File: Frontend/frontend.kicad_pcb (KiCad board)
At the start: 4 copper layers, 100 x 100.2 mm, 355 parts, among them J1 VOCM, J10 SWD, J11 APWR, J2 BNC, J3 UMC, J4 UMC, J5 VOCM, J6 BNC, J7 UMC, J8 UMC, J9 PCIEx4 EDGE, K1 HE3600, K2 EE2-5NU, K3 HE3600, K4 HE3600, K5 EE2-5NU, K6 HE3600, Q1 ULN2003AD, U1 MCP9700T-E/TT, U10 ADA4817-1ACPZ, U11 MAX4567EEE, U12 MAX4567EEE, U13 MAX4567EEE, U14 AD8003ACPZ, U15 LMH6552SD, U16 MC33078DGK, U17 MAX5725AAUP, U18 STM32F030C8T, U19 MC33078DGK, U2 ADA4817-1ACPZ, U20 MC33078DGK, U21 MC33078DGK, U22 MC33078DGK, U23 LM317S, U24 MCP9700T-E/TT, U25 L78M05CDT, U26 TLV70233DSE, U27 MCP9700T-E/TT, U28 MC79M05CDT, U3 MAX4567EEE, U4 MAX4567EEE, U5 MAX4567EEE, U6 AD8003ACPZ, U7 LMH6552SD, U8 MC33078DGK, U9 MCP9700T-E/TT

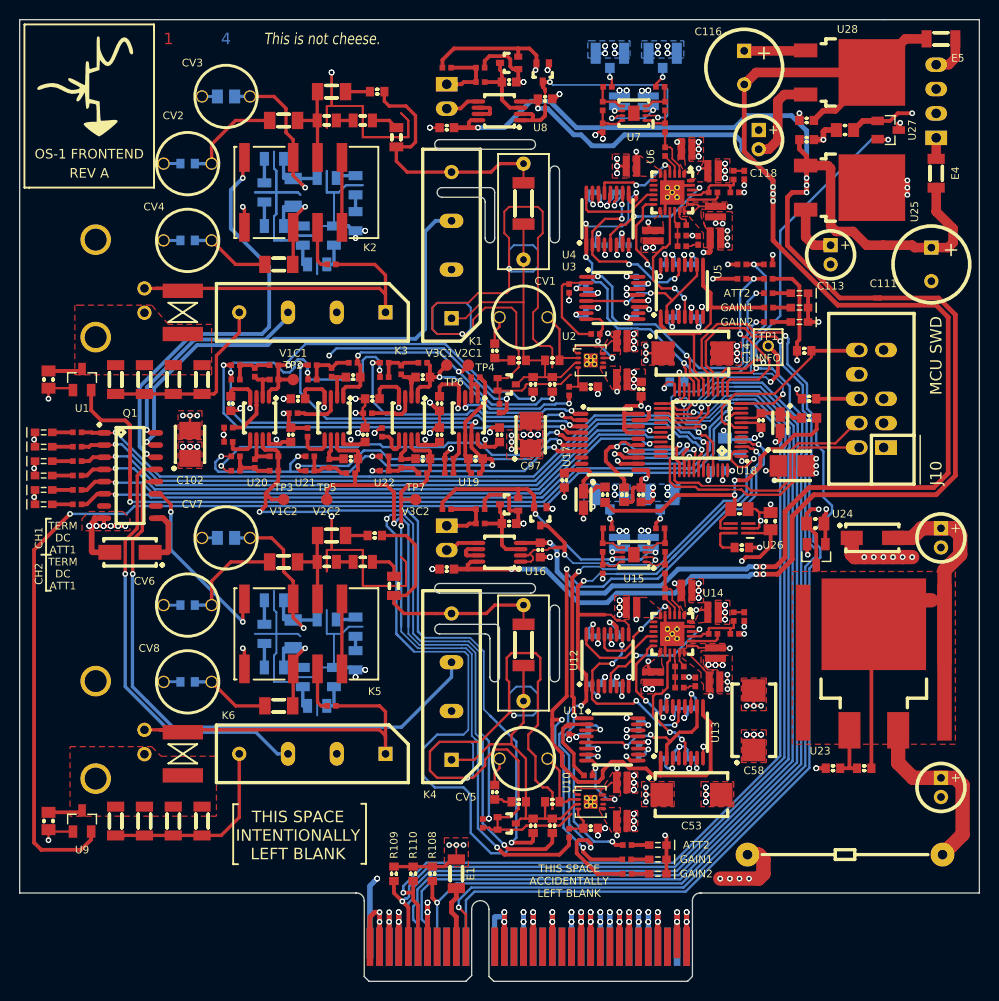
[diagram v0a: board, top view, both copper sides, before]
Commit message: Add testpoints
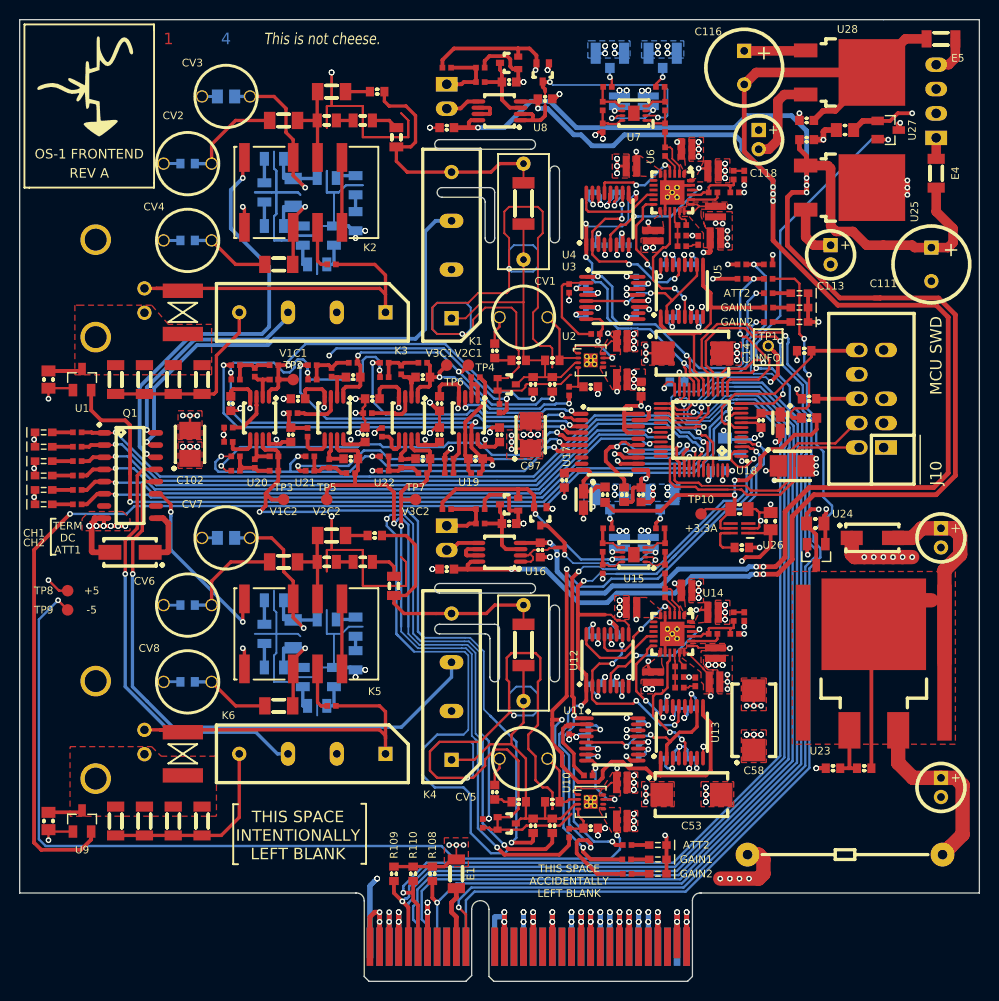
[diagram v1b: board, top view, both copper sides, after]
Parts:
- added TP10: +3.3A, conn-test:TEST-SMD-SMALL, F.Cu at (133.0, 69.5)
- added TP8: +5, conn-test:TEST-SMD-SMALL, F.Cu at (67.0, 77.5)
- added TP9: -5, conn-test:TEST-SMD-SMALL, F.Cu at (67.0, 79.5)
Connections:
- R91 pad 1: +3.3 -> /Microcontroller/3V3ADC
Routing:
- net -5: track 270.6 -> 361.1 mm, vias 26 -> 27
- net /Microcontroller/3V3ADC: track 6.73 -> 25.7 mm, vias 0 -> 2
- net +3.3: track 102.7 -> 92.7 mm
- net +3.3A: track 33.8 -> 37.1 mm
- net +5: track 507.5 -> 509.9 mm, vias 36 -> 37
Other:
- board text added: "+3.3A"
- board text added: "+5"
- board text added: "-5"

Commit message: Digital decoupling/termination tweaks
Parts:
- added E6: 600, IPC7351-Nominal:INDC1005X60, F.Cu at (103.5, 106.5)
- added E7: 600, IPC7351-Nominal:INDC1005X60, F.Cu at (102.0, 106.5)
- added R149: 100, IPC7351-Nominal:RESC1005X40, B.Cu at (143.5, 89.0)
- added R150: 100, IPC7351-Nominal:RESC1005X40, B.Cu at (144.2, 91.5)
- added R151: 100, IPC7351-Nominal:RESC1005X40, B.Cu at (142.8, 91.5)
- added R152: 100, IPC7351-Nominal:RESC1005X40, B.Cu at (145.2, 89.0)
- C83, C84, C85, C86, C89: footprint IPC7351-Nominal:CAPC1608X55 -> IPC7351-Nominal:CAPC1005X55
- E2, E3: value BEAD-0603 -> 600; footprint IPC7351-Nominal:INDC1608X95 -> IPC7351-Nominal:INDC1005X60
- R108, R109, R110: footprint IPC7351-Nominal:RESC1608X50 -> IPC7351-Nominal:RESC1005X40
- moved R109 3.40 mm to (102.0, 103.8)
- moved R110 3.29 mm to (103.5, 103.8)
- moved E3 0.87 mm to (143.5, 60.0), turned to 90 degrees
- moved C85 0.50 mm to (137.8, 62.5)
- moved C82 0.50 mm to (136.0, 62.5)
- moved C83 0.50 mm to (127.2, 56.5)
- moved R108 0.50 mm to (105.0, 106.5)
- moved C86 0.39 mm to (130.8, 56.0)
- moved C89 0.25 mm to (139.0, 59.8), turned to 270 degrees
- moved C84 0.20 mm to (134.9, 65.0)
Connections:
- C89 pad 1: GND -> /Microcontroller/3V3ADC
- C89 pad 2: /Microcontroller/3V3ADC -> GND
- J9 pad B5: /Microcontroller/SDA -> Net-(E7-Pad1)
- J9 pad B6: /Microcontroller/SCL -> Net-(E6-Pad1)
- U18 pad 25: /Microcontroller/#SS -> /Microcontroller/#CSEXT
- U18 pad 26: /Microcontroller/SCK -> /Microcontroller/SCKEXT
- U18 pad 27: /Microcontroller/MISO -> /Microcontroller/MISOEXT
- U18 pad 28: /Microcontroller/MOSI -> /Microcontroller/MOSIEXT
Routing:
- net /Microcontroller/MISO: track 104.2 -> 54.2 mm, vias 1 -> 0
- net /Microcontroller/MISOEXT: track 0.00 -> 49.7 mm, vias 0 -> 1
- net /Microcontroller/#CSEXT: track 0.00 -> 47.3 mm, vias 0 -> 1
- net /Microcontroller/SCK: track 101.6 -> 54.6 mm, vias 1 -> 0
- net /Microcontroller/SCKEXT: track 0.00 -> 46.9 mm, vias 0 -> 1
- net /Microcontroller/MOSI: track 103.4 -> 56.6 mm, vias 1 -> 0
- net /Microcontroller/MOSIEXT: track 0.00 -> 46.1 mm, vias 0 -> 1
- net /Microcontroller/#SS: track 104.5 -> 58.8 mm, vias 2 -> 1
- net /Microcontroller/SCL: track 103.4 -> 94.2 mm
- net Net-(E7-Pad1): track 0.00 -> 7.86 mm
- net Net-(E6-Pad1): track 0.00 -> 7.65 mm
- net /Microcontroller/SDA: track 105.8 -> 98.4 mm
- net /Microcontroller/#PERST: track 110.4 -> 113.2 mm
- net +3.3: track 92.7 -> 94.8 mm
- net /Microcontroller/#IRQ: track 107.7 -> 109.5 mm
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
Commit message: Schematic cleanup
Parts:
- U18: value STM32F030C8T -> STM32V030C8T
- moved R109 0.25 mm to (102.0, 103.5)
- moved R110 0.25 mm to (103.5, 103.5)
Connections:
- net /Microcontroller/#CSEXT renamed /Microcontroller/F_#SS
- net /Microcontroller/+5VMON renamed Net-(R90-Pad2)
- net /Microcontroller/-5VMON renamed Net-(R91-Pad2)
- net /Microcontroller/3V3ADC renamed Net-(C88-Pad1)
- net /Microcontroller/MISOEXT renamed /Microcontroller/F_MISO
- net /Microcontroller/MOSIEXT renamed /Microcontroller/F_MOSI
- net /Microcontroller/SCKEXT renamed /Microcontroller/F_SCK
- net /Microcontroller/TX renamed Net-(TP1-Pad1)
- E6 pad 1: Net-(E6-Pad1) -> /Microcontroller/SCL
- E6 pad 2: /Microcontroller/SCL -> /Microcontroller/F_SCL
- E7 pad 1: Net-(E7-Pad1) -> /Microcontroller/SDA
- E7 pad 2: /Microcontroller/SDA -> /Microcontroller/F_SDA
- J9 pad B5: Net-(E7-Pad1) -> /Microcontroller/SDA
- J9 pad B6: Net-(E6-Pad1) -> /Microcontroller/SCL
- R109 pad 2: /Microcontroller/SDA -> /Microcontroller/F_SDA
- R110 pad 2: /Microcontroller/SCL -> /Microcontroller/F_SCL
- U18 pad 21: /Microcontroller/SCL -> /Microcontroller/F_SCL
- U18 pad 22: /Microcontroller/SDA -> /Microcontroller/F_SDA
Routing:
- net /Microcontroller/F_SDA: track 0.00 -> 98.6 mm, vias 0 -> 2
- net /Microcontroller/F_SCL: track 0.00 -> 94.6 mm, vias 0 -> 2
- net /Microcontroller/SDA: track 98.4 -> 7.86 mm, vias 2 -> 0
- net /Microcontroller/SCL: track 94.2 -> 7.65 mm, vias 2 -> 0
- net Net-(E7-Pad1): track 7.86 -> 0.00 mm
- net Net-(E6-Pad1): track 7.65 -> 0.00 mm

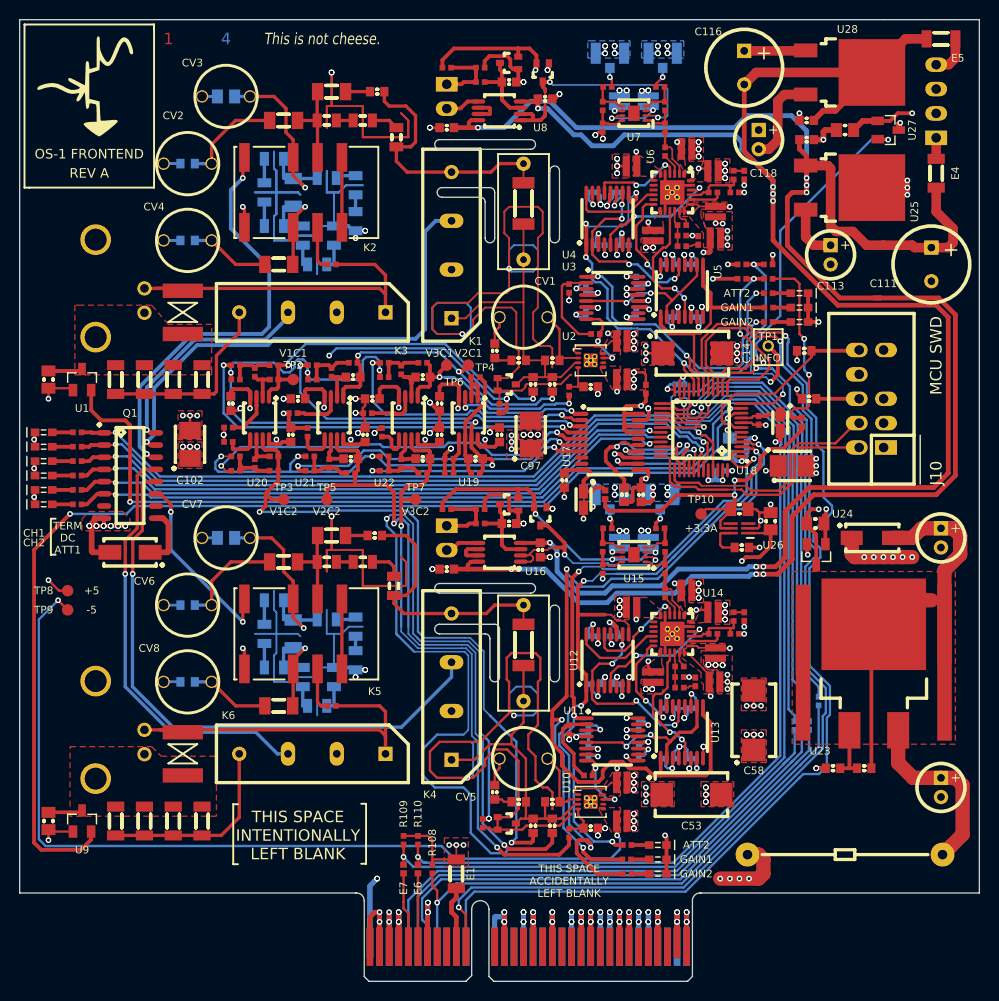
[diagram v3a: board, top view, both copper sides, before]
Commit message: Cleanup offset compensation system
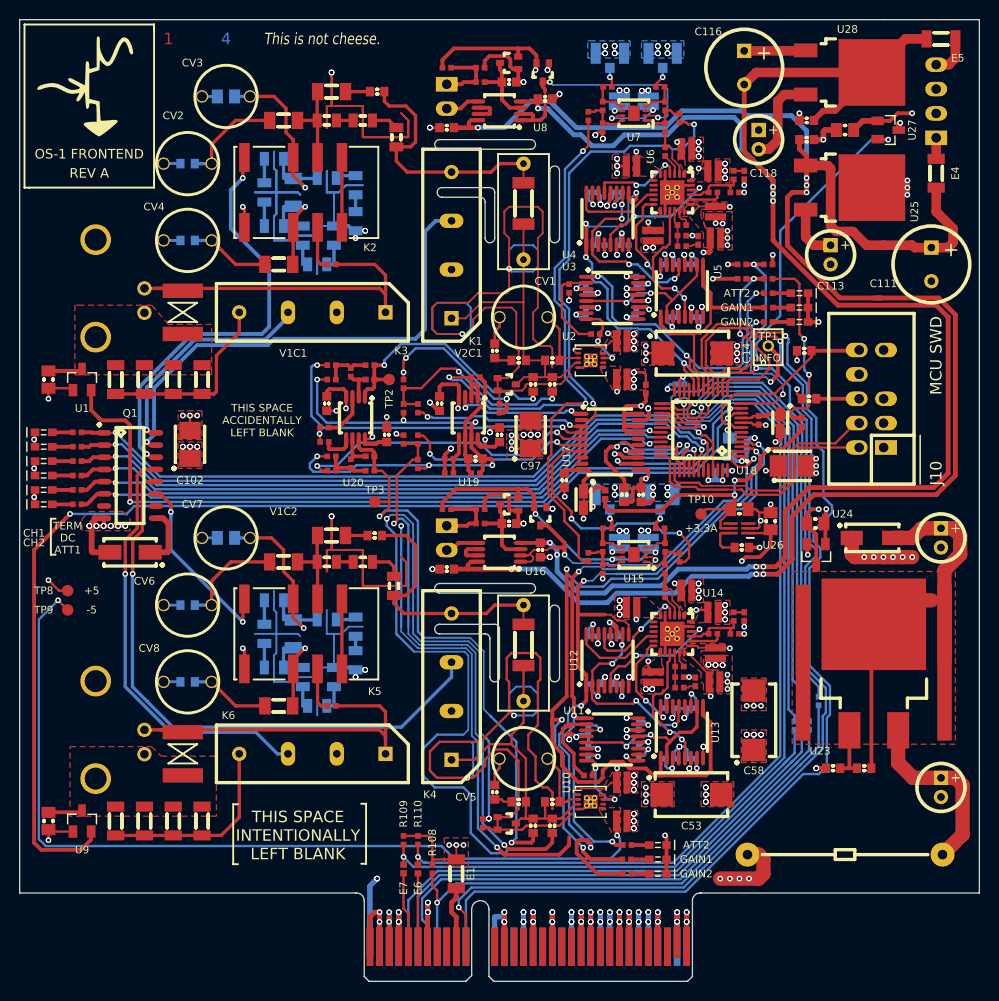
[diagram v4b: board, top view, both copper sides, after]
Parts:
- removed C10, C100, C101, C105, C106, C49, C93, C94, C95, C96: 100n, IPC7351-Nominal:CAPC1608X55
- removed R129, R139, R141: 20k, IPC7351-Nominal:RESC1005X40
- removed R130, R133, R134, R140, R142, R143, R144: 5k6, IPC7351-Nominal:RESC1005X40
- removed R135, R137: 10k, IPC7351-Nominal:RESC1005X40
- removed R136, R138: 100, IPC7351-Nominal:RESC1005X40
- removed TP4: V2C1, conn-test:TEST-SMD-SMALL
- removed TP5: V2C2, conn-test:TEST-SMD-SMALL
- removed TP6: V3C1, conn-test:TEST-SMD-SMALL
- removed TP7: V3C2, conn-test:TEST-SMD-SMALL
- removed U21, U22: MC33078DGK, IPC7351-Nominal:SOP65P490X109-8
- added R153: 10k, IPC7351-Nominal:RESC1005X40, F.Cu at (130.8, 74.0)
- added R154: 20k, IPC7351-Nominal:RESC1005X40, F.Cu at (121.2, 74.0)
- R124: value 680 -> 10k
- R125: value 10k -> 20k
- R126: value 680 -> 820
- R128: value 5k6 -> 820
- R23: value 150 -> 10k
- R67: value 150 -> 20k
- U18: value STM32V030C8T -> STM32F030C8T
- moved R67 74.7 mm to (121.2, 28.1)
- moved R23 30.7 mm to (130.8, 28.2)
- moved R127 14.1 mm to (103.5, 64.3), turned to 90 degrees
- moved R123 11.9 mm to (103.5, 58.5), turned to 270 degrees
- moved R125 11.7 mm to (102.0, 58.5), turned to 90 degrees
- moved R126 10.8 mm to (102.0, 56.0), turned to 270 degrees
- moved R124 10.5 mm to (103.5, 61.8), turned to 90 degrees
- moved R128 10.3 mm to (102.0, 61.8)
- moved C104 10.0 mm to (94.0, 58.0)
- moved C90 10.0 mm to (98.5, 55.5)
- moved C91 10.0 mm to (98.5, 63.5)
- moved C99 10.0 mm to (100.2, 61.2)
- moved R111 10.0 mm to (94.5, 54.0)
- moved R112 10.0 mm to (98.5, 54.0)
- moved R113 10.0 mm to (94.5, 65.0)
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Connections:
- net Net-(R90-Pad2) renamed /Microcontroller/P5SENSE
- net Net-(R91-Pad2) renamed /Microcontroller/N5SENSE
- R123 pad 1: Net-(R123-Pad1) -> /Channel1/VOS2
- R124 pad 1: /Channel1/VOS2 -> /Channel2/VOS2
- R124 pad 2: Net-(R123-Pad1) -> /Microcontroller/LevelShifters/VOS2_CH2_IN
- R125 pad 1: Net-(R125-Pad1) -> -2.5
- R125 pad 2: /Microcontroller/LevelShifters/VOS2_CH2_IN -> /Channel1/VOS2
- R126 pad 1: /Channel2/VOS2 -> GND
- R126 pad 2: Net-(R125-Pad1) -> /Channel1/VOS2
- R127 pad 1: Net-(R123-Pad1) -> -2.5
- R127 pad 2: -2.5 -> /Channel2/VOS2
- R128 pad 1: Net-(R123-Pad1) -> GND
- R128 pad 2: Net-(C93-Pad2) -> /Channel2/VOS2
- R23 pad 1: Net-(C10-Pad1) -> Net-(R23-Pad1)
- R27 pad 1: Net-(R27-Pad1) -> Net-(R23-Pad1)
- R28 pad 2: Net-(R27-Pad1) -> Net-(R23-Pad1)
- R67 pad 1: Net-(C49-Pad1) -> Net-(R39-Pad1)
- R67 pad 2: /Channel2/VOS3 -> +2.5
- U10 pad 4: Net-(C49-Pad1) -> GND
- U17 pad 2: /Microcontroller/LevelShifters/VOS3_CH1_IN -> /Channel1/VOS3
- U17 pad 7: /Microcontroller/LevelShifters/VOS3_CH2_IN -> /Channel2/VOS3
- U2 pad 4: Net-(C10-Pad1) -> GND
- U7 pad 1: Net-(R27-Pad1) -> Net-(R23-Pad1)
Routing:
- net +2.5: track 3.88 -> 76.1 mm, vias 0 -> 3
- net (no net): track 8.10 -> 57.7 mm, vias 0 -> 2
- net -2.5: track 98.6 -> 53.6 mm, vias 8 -> 6
- net /Channel2/VOS3: track 63.9 -> 26.6 mm
- net GND: track 1254.0 -> 1217.0 mm, vias 421 -> 403
- net /Microcontroller/LevelShifters/VOS3_CH1_IN: track 27.9 -> 0.00 mm, vias 2 -> 0
- net /Microcontroller/LevelShifters/VOS3_CH2_IN: track 23.8 -> 0.00 mm, vias 2 -> 0
- net /Channel1/VOS3: track 23.2 -> 46.7 mm
- net /Microcontroller/LevelShifters/VOS2_CH1_IN: track 34.7 -> 17.8 mm
- net /Microcontroller/LevelShifters/VOS2_CH2_IN: track 32.9 -> 19.7 mm
- net /Channel2/VOS1: track 72.9 -> 61.2 mm
- net /Microcontroller/LevelShifters/VOS1_CH2_IN: track 41.9 -> 31.6 mm
- net /Channel1/VOS1: track 36.4 -> 26.4 mm
- net /Channel1/VOS2: track 30.9 -> 22.0 mm, vias 3 -> 2
- net /Microcontroller/LevelShifters/VOS1_CH1_IN: track 44.2 -> 36.0 mm
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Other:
- board text removed: "V2C2"
- board text removed: "V3C1"
- board text removed: "V3C2"

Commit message: Even more layout tweaks
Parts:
- added C10: 2u2, IPC7351-Nominal:CAPMP2013X120, F.Cu at (103.5, 58.5)
- added C19: 2u2, IPC7351-Nominal:CAPMP2013X120, F.Cu at (102.0, 64.2)
- added TP11: S2, conn-test:TEST-SMD-SMALL, B.Cu at (131.2, 45.0)
- added TP12: S2, conn-test:TEST-SMD-SMALL, B.Cu at (131.5, 91.8)
- added TP13: S2, conn-test:TEST-SMD-SMALL, B.Cu at (128.0, 33.2)
- added TP14: S2, conn-test:TEST-SMD-SMALL, B.Cu at (128.2, 80.0)
- added TP4: BUFFER, conn-test:TEST-SMD-SMALL, B.Cu at (123.5, 52.0)
- added TP5: BUFFER, conn-test:TEST-SMD-SMALL, B.Cu at (123.5, 97.5)
- added TP6: S1, conn-test:TEST-SMD-SMALL, B.Cu at (128.8, 46.5)
- added TP7: S1, conn-test:TEST-SMD-SMALL, B.Cu at (128.8, 92.8)
- G***: moved to B.Cu
- R100, R107, R89: footprint IPC7351-Nominal:RESC1608X50 -> IPC7351-Nominal:RESC1005X40
- R108, R109, R110: value 47k -> 10k
- moved G*** 102.4 mm to (154.0, 82.2), turned to 180 degrees
- moved R74 2.79 mm to (119.2, 94.8), turned to 90 degrees
- moved R123 2.50 mm to (105.5, 60.0), turned to 0 degrees
- moved R30 2.06 mm to (120.0, 50.2)
- moved R34 1.25 mm to (119.2, 44.8), turned to 90 degrees
- moved TP3 0.90 mm to (98.5, 69.0)
- moved R78 0.75 mm to (119.2, 91.2), turned to 90 degrees
- moved R107 0.50 mm to (143.8, 57.5), turned to 0 degrees
- turned R89 to 90 degrees
- turned R100 to 0 degrees
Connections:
- net Net-(E1-Pad2) renamed /3V3SB
- net Net-(TP1-Pad1) renamed /Microcontroller/DBG_TX
- R100 pad 1: /Microcontroller/#RST -> +3.3
- R100 pad 2: +3.3 -> /Microcontroller/#RST
- R107 pad 1: /Microcontroller/SWO -> +3.3
- R107 pad 2: +3.3 -> /Microcontroller/SWO
- R89 pad 1: /Microcontroller/#CSDAC -> +3.3
- R89 pad 2: +3.3 -> /Microcontroller/#CSDAC
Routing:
- net GND: track 1217.0 -> 1339.0 mm, vias 403 -> 458
- net (no net): track 57.7 -> 0.50 mm, vias 2 -> 0
- net -8: track 246.6 -> 237.2 mm, vias 13 -> 10
- net /Microcontroller/CH2_GAIN1: track 102.2 -> 94.6 mm, vias 4 -> 5
- net /Channel2/ATT2: track 64.5 -> 70.5 mm
- net +2.5: track 76.1 -> 70.6 mm
- net +5: track 509.9 -> 515.4 mm
- net -5: track 361.1 -> 355.7 mm, vias 27 -> 29
- net +12: track 71.9 -> 77.0 mm
- net Net-(R74-Pad2): track 8.46 -> 4.56 mm
- net +8: track 250.2 -> 246.6 mm, vias 13 -> 10
- net -2.5: track 53.6 -> 56.9 mm
- net /Channel1/VOS2: track 22.0 -> 25.3 mm
- net /Microcontroller/CH2_GAIN2: track 75.3 -> 78.1 mm
- net VRELAY: track 250.8 -> 253.6 mm, vias 8 -> 16
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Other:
- board text added: "+"
- board text added: "+12"
- board text added: "-8 GND GND +8"
- board text added: "12V"
- board text added: "13"
- board text added: "37"
- board text added: "3V3"
- board text added: "CHAN 1"
- board text added: "CHAN 2"
- board text added: "DS10~~12"
- board text added: "DS1~~6"
- board text added: "DS7~~9"
- board text added: "GND"
- board text added: "MISO"
- board text added: "MOSI"
- board text added: "R101~~103"
- board text added: "R104~~106"
- board text added: "R94~~99"
- board text added: "SCK"
- board text added: "SCL"
- board text added: "SDA"
- board text added: "SWCLK"
- board text added: "SWDIO"
- board text added: "Vocm DRIVE"
- board text added: "~IRQ"
- board text added: "~PERST"
- board text added: "~RST"
- board text added: "~SS"
- board text removed: "+3.3A"
- board text removed: "THIS UP"
- board text removed: "V1C1"
- board text removed: "V1C2"
- board text removed: "V2C1"
- board text removed: "WAY"
